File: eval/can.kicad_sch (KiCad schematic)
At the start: 1 part, among them U7 TCAN3413DR

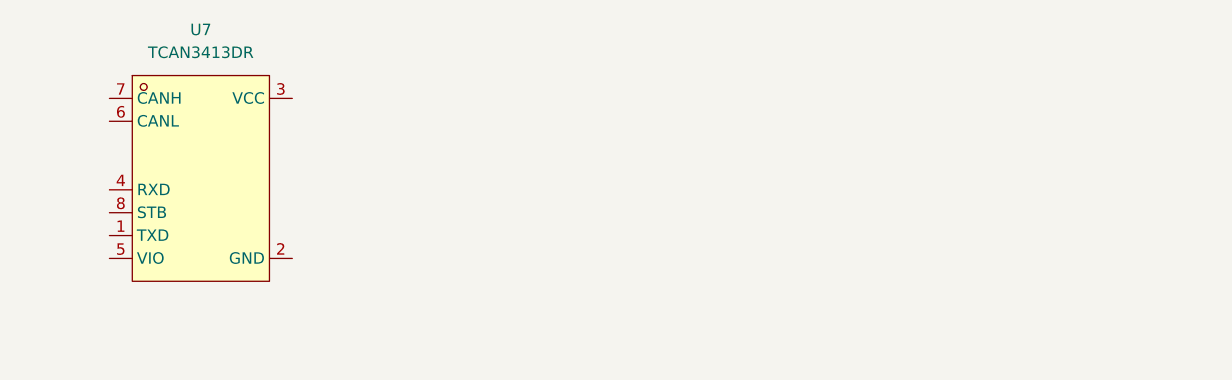
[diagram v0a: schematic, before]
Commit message: add CAN to sch
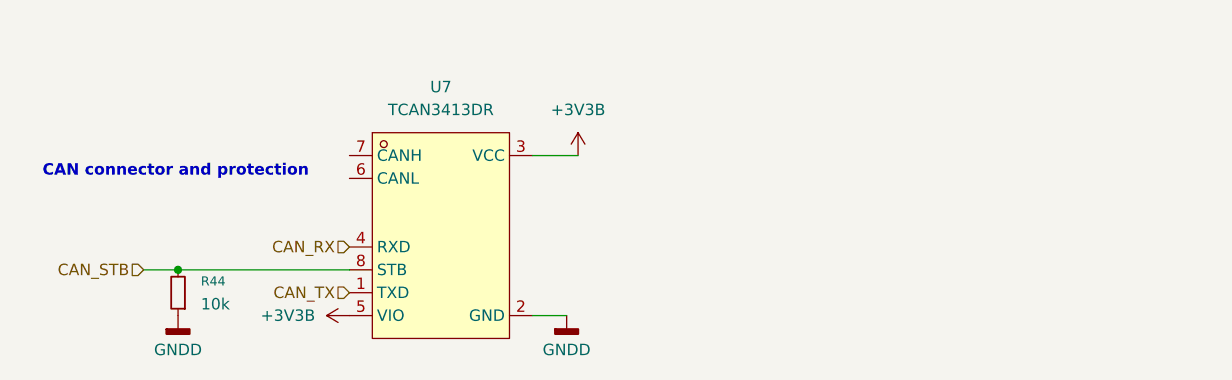
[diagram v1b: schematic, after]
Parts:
- added R44: 10k, symbol Device:R_Small
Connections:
- net CAN_TX: now reaches U7.1 (TXD)
- net GNDD: now reaches U7.2 (GND)
- net GNDD: now also R44.1
- net +3V3B: now reaches U7.3 (VCC)
- net +3V3B: now also U7.5 (VIO)
- net CAN_RX: now reaches U7.4 (RXD)
- net CAN_STB: now reaches U7.8 (STB)
- net CAN_STB: now also R44.2
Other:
- note added: "CAN connector and protection"
- moved on the sheet: U7

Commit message: [Layout] complete loop, root and buck layout
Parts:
- R44: footprint (none) -> Resistor_SMD:R_0603_1608Metric
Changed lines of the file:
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@@
 			)
 		)
-		(property "Footprint" ""
+		(property "Footprint" "Resistor_SMD:R_0603_1608Metric"
 			(at 48.26 63.5 0)
 			(hide yes)

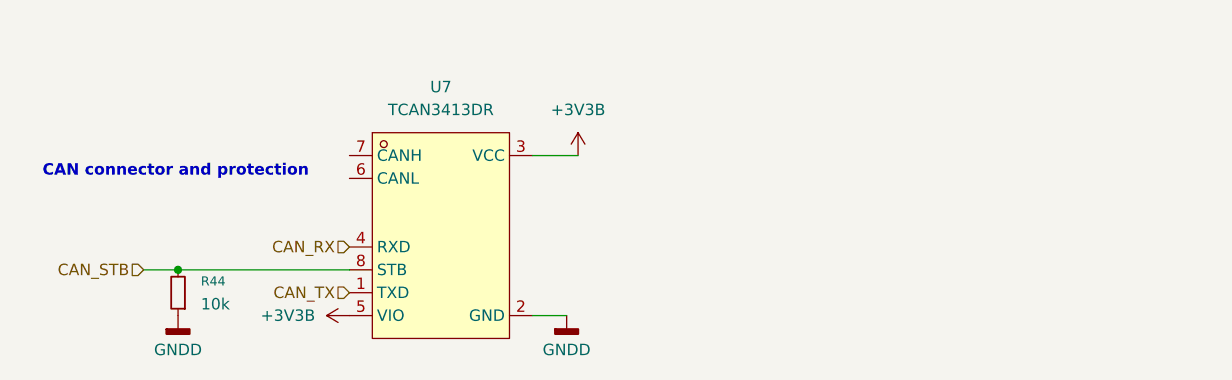
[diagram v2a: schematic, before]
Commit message: [layout] trying to put all components in limit dimention
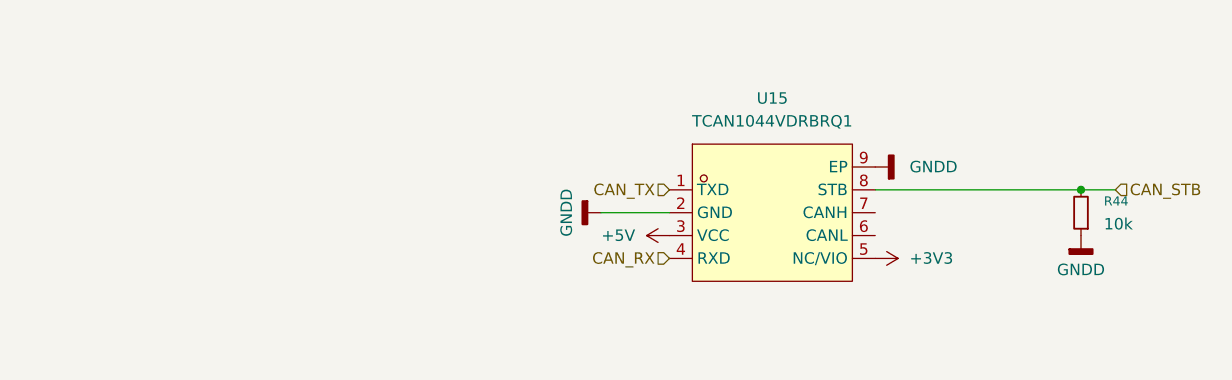
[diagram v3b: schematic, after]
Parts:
- removed U7: TCAN3413DR, EasyEDA:SOP-8_L4.9-W3.9-P1.27-LS6.0-BL-1, symbol EasyEDA:TCAN3413DR
- added U15: TCAN1044VDRBRQ1, EasyEDA:VSON-8_L3.0-W3.0-P0.65-BR-EP, symbol EasyEDA:TCAN1044VDRBRQ1
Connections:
- net CAN_RX: now also U15.4 (RXD)
- net CAN_STB: now also U15.8 (STB)
- net CAN_TX: now also U15.1 (TXD)
- net GNDD: now also U15.2 (GND), U15.9 (EP)
- new net +3V3: U15.5 (NC/VIO)
- new net +5V: U15.3 (VCC)
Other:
- note removed: "CAN connector and protection"
